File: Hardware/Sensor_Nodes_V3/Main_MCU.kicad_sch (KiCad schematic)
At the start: 21 parts, among them J2 Conn_01x27_Socket, J3 Conn_01x27_Socket, U2 STM32G474RBTx, U3 MCP2542FDxMF, U4 MCP2542FDxMF

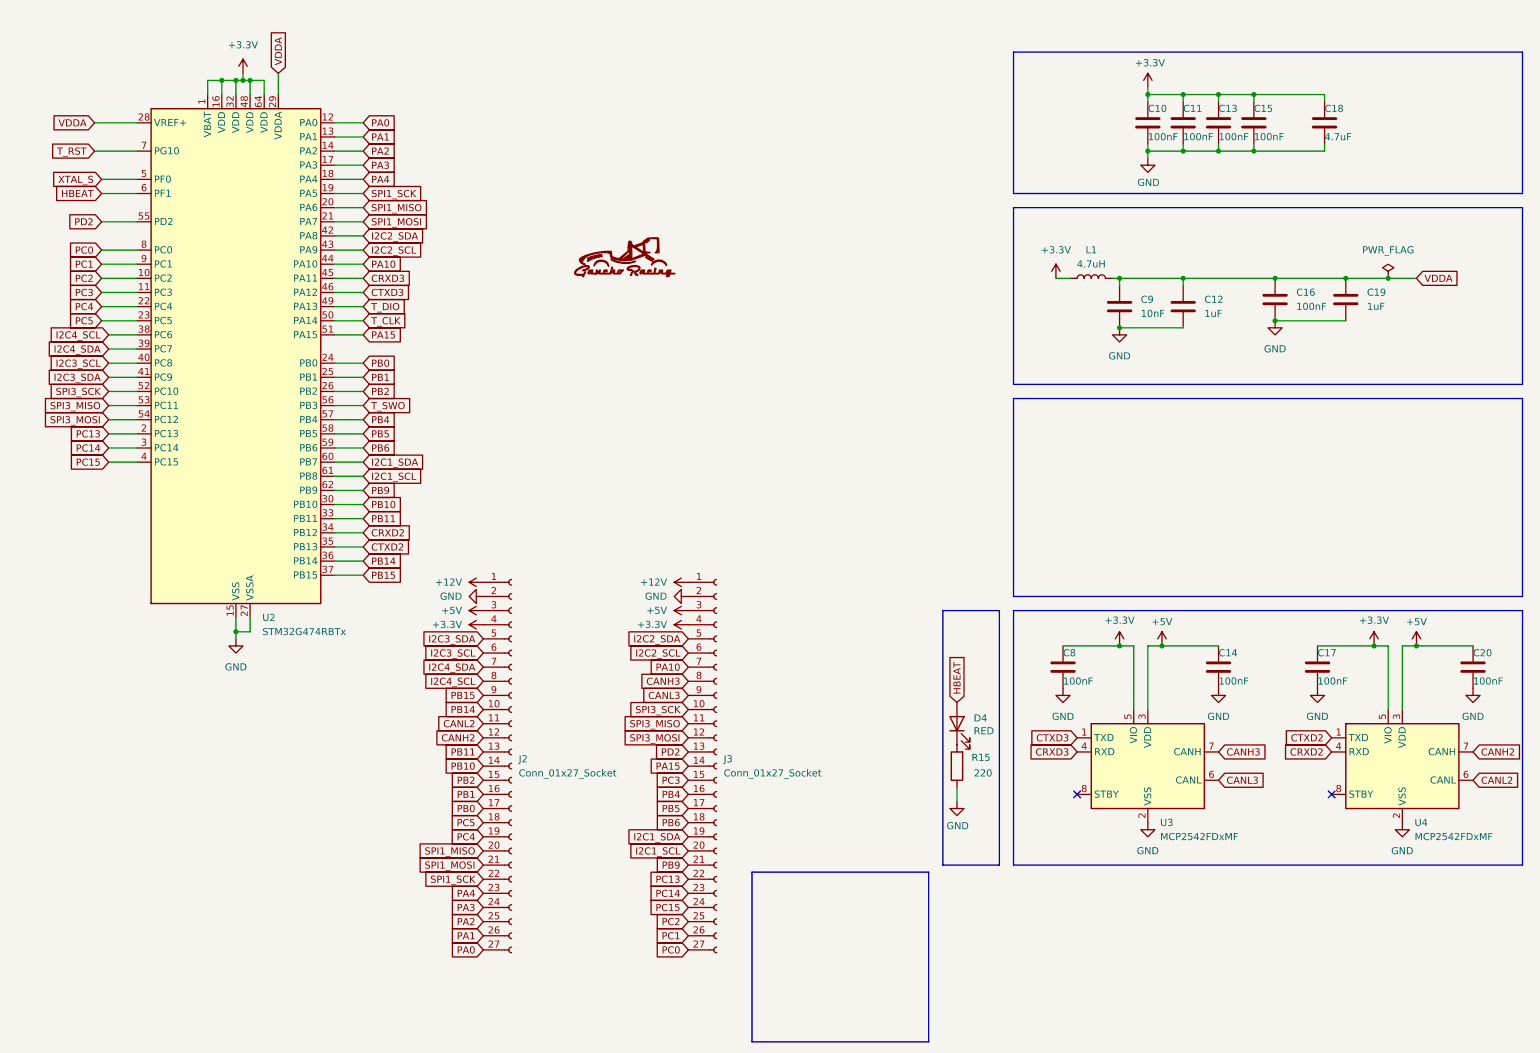
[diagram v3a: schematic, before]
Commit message: fixed placement, added some decals, now using clock from stlink
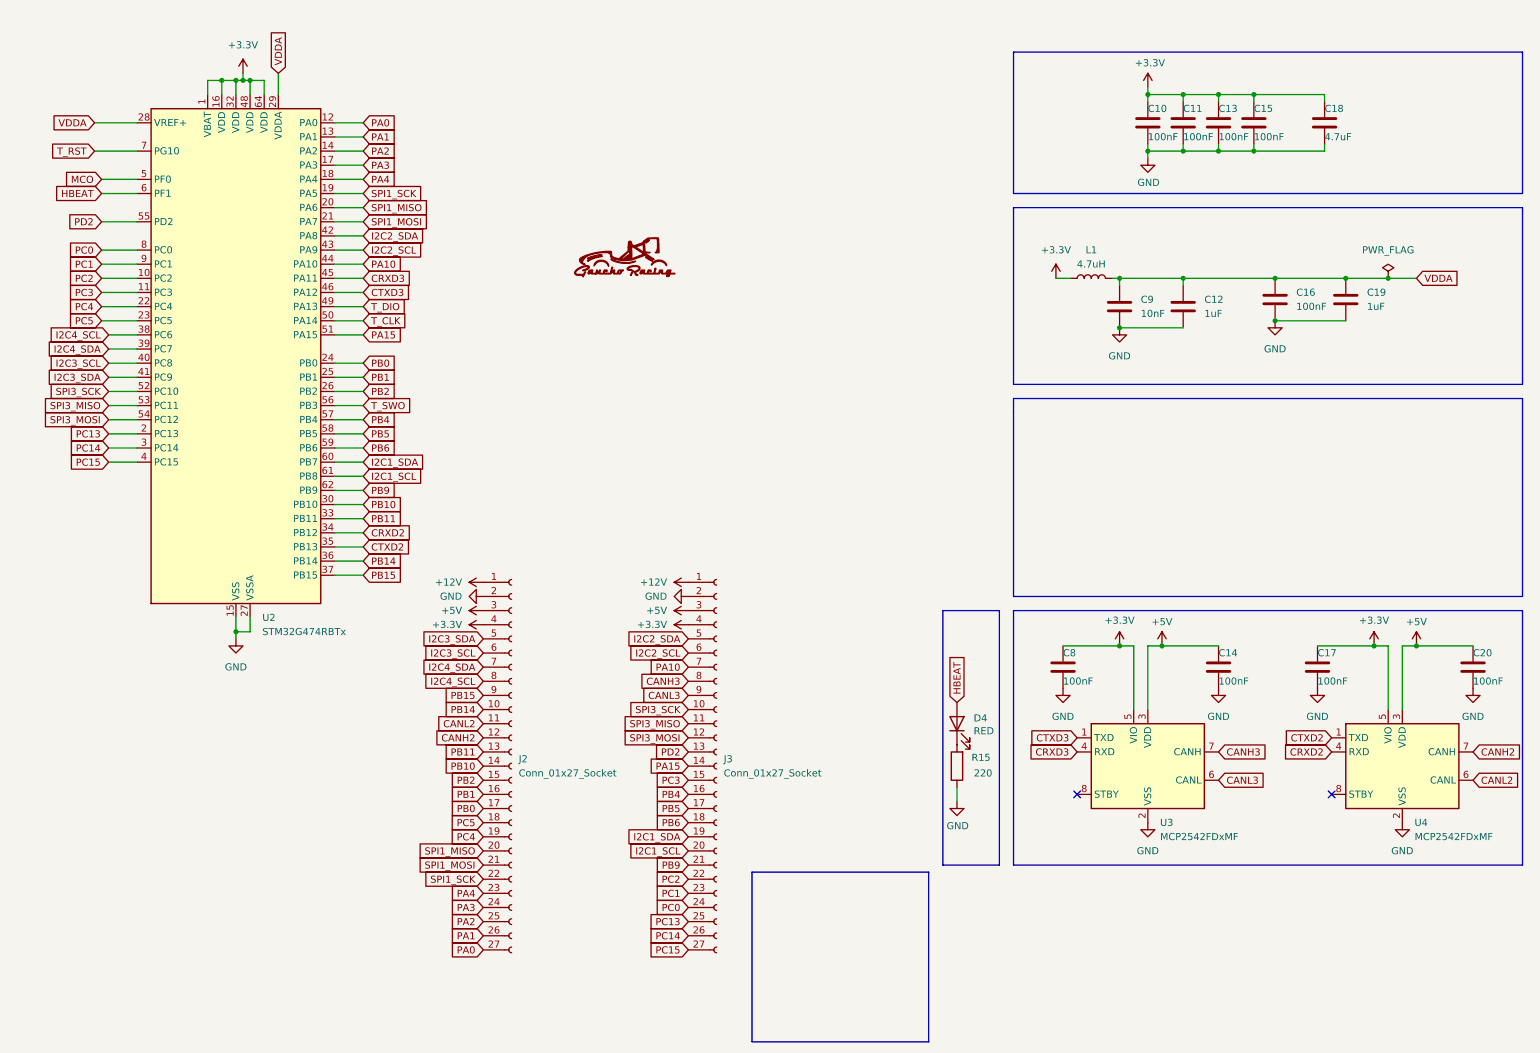
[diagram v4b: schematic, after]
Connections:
- net PC0: now also J3.24 (Pin_24); no longer J3.27 (Pin_27)
- net PC1: now also J3.23 (Pin_23); no longer J3.26 (Pin_26)
- net PC13: now also J3.25 (Pin_25); no longer J3.22 (Pin_22)
- net PC14: now also J3.26 (Pin_26); no longer J3.23 (Pin_23)
- net PC15: now also J3.27 (Pin_27); no longer J3.24 (Pin_24)
- net PC2: now also J3.22 (Pin_22); no longer J3.25 (Pin_25)
- net XTAL_S renamed MCO

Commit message: fixed the CAN issue and rerouted some things. Added a solder bridge for Vref so that there is a choice of using it or not.
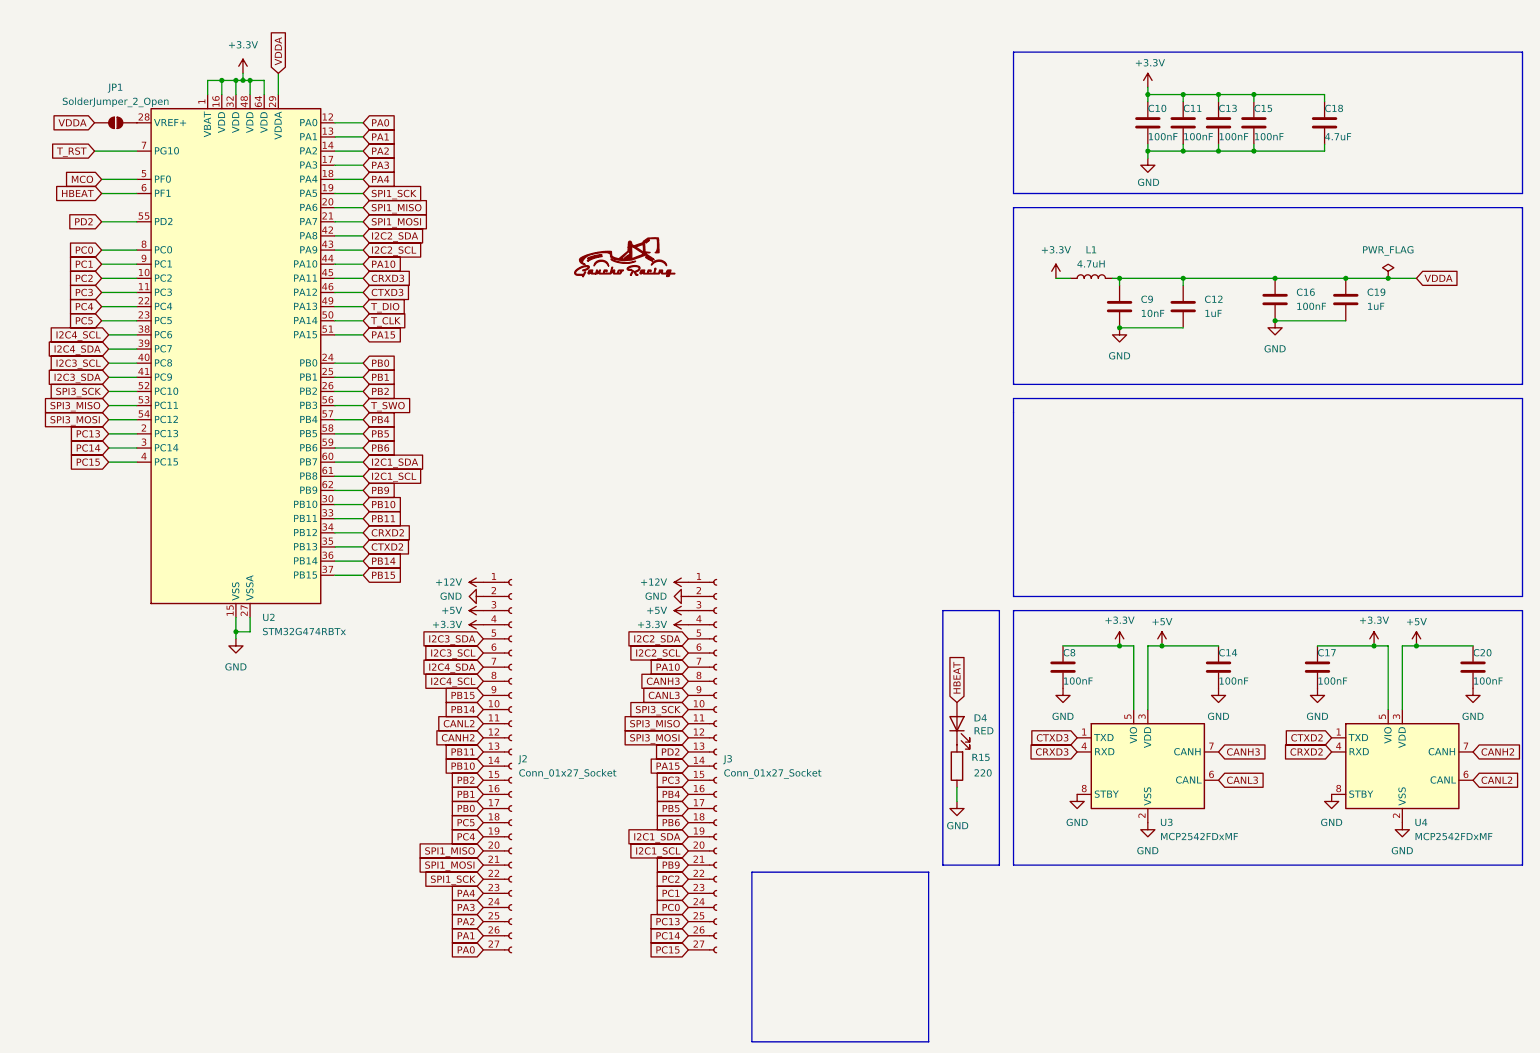
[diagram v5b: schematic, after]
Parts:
- added JP1: SolderJumper_2_Open, Jumper:SolderJumper-2_P1.3mm_Open_TrianglePad1.0x1.5mm, symbol Jumper:SolderJumper_2_Open
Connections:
- net GND: now also U3.8 (STBY), U4.8 (STBY)
- net VDDA: now also JP1.1 (A); no longer U2.28 (VREF+)
- new net: JP1.2 (B), U2.28 (VREF+)
- no-connect marks 2 -> 0
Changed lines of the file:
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@@
 		(color 0 0 0 0)
 	)
-	(no_connect
-		(at 247.65 152.4)
-	)
-	(no_connect
-		(at 201.93 152.4)
-	)
 	(wire
 		(pts
@@
 		)
 	)
-	(wire
-		(pts
-			(xy 25.4 31.75) (xy 33.02 31.75)
-		)
-		(stroke
-			(width 0)
-			(type default)
-		)
-	)
 	(polyline
 		(pts
@@
 	)
 	(symbol
+		(lib_id "Jumper:SolderJumper_2_Open")
+		(at 29.21 31.75 0)
+		(unit 1)
+		(exclude_from_sim yes)
+		(in_bom no)
+		(on_board yes)
+		(dnp no)
+		(fields_autoplaced yes)
+		(property "Reference" "JP1"
+			(at 29.21 25.4 0)
+			(effects
+				(font
+					(size 1.27 1.27)
+				)
+			)
+		)
+		(property "Value" "SolderJumper_2_Open"
+			(at 29.21 27.94 0)
+			(effects
+				(font
+					(size 1.27 1.27)
+				)
+			)
+		)
+		(property "Footprint" "Jumper:SolderJumper-2_P1.3mm_Open_TrianglePad1.0x1.5mm"
+			(at 29.21 31.75 0)
+			(effects
+				(font
+					(size 1.27 1.27)
+				)
+				(hide yes)
+			)
+		)
+		(property "Datasheet" "~"
+			(at 29.21 31.75 0)
+			(effects
+				(font
+					(size 1.27 1.27)
+				)
+				(hide yes)
+			)
+		)
+		(property "Description" "Solder Jumper, 2-pole, open"
+			(at 29.21 31.75 0)
+			(effects
+				(font
+					(size 1.27 1.27)
+				)
+				(hide yes)
+			)
+		)
+		(pin "2"
+		)
+		(pin "1"
+		)
+		(instances
+			(project ""
+				(path "/7b4e8e38-4440-451f-8c12-a5c49d6e3525/466e2466-e768-4b2c-901e-6531e50d4122"
+					(reference "JP1")
+					(unit 1)
+				)
+			)
+		)
+	)
+	(symbol
 		(lib_id "Device:C")
 		(at 214.63 31.75 0)
@@
 	)
 	(symbol
+		(lib_id "power:GND")
+		(at 201.93 152.4 0)
+		(unit 1)
+		(exclude_from_sim no)
+		(in_bom yes)
+		(on_board yes)
+		(dnp no)
+		(fields_autoplaced yes)
+		(property "Reference" "#PWR056"
+			(at 201.93 158.75 0)
+			(effects
+				(font
+					(size 1.27 1.27)
+				)
+				(hide yes)
+			)
+		)
+		(property "Value" "GND"
+			(at 201.93 157.48 0)
+			(effects
+				(font
+					(size 1.27 1.27)
+				)
+			)
+		)
+		(property "Footprint" ""
+			(at 201.93 152.4 0)
+			(effects
+				(font
+					(size 1.27 1.27)
+				)
+				(hide yes)
+			)
+		)
+		(property "Datasheet" ""
+			(at 201.93 152.4 0)
+			(effects
+				(font
+					(size 1.27 1.27)
+				)
+				(hide yes)
+			)
+		)
+		(property "Description" "Power symbol creates a global label with name \"GND\" , ground"
+			(at 201.93 152.4 0)
+			(effects
+				(font
+					(size 1.27 1.27)
+				)
+				(hide yes)
+			)
+		)
+		(pin "1"
+		)
+		(instances
+			(project ""
+				(path "/7b4e8e38-4440-451f-8c12-a5c49d6e3525/466e2466-e768-4b2c-901e-6531e50d4122"
+					(reference "#PWR056")
+					(unit 1)
+				)
+			)
+		)
+	)
+	(symbol
 		(lib_id "Device:C")
 		(at 227.33 31.75 0)
@@
 					(unit 1)
 				)
+			)
+		)
+	)
+	(symbol
+		(lib_id "power:GND")
+		(at 247.65 152.4 0)
+		(unit 1)
+		(exclude_from_sim no)
+		(in_bom yes)
+		(on_board yes)
+		(dnp no)
+		(fields_autoplaced yes)
+		(property "Reference" "#PWR057"
+			(at 247.65 158.75 0)
+			(effects
+				(font
+					(size 1.27 1.27)
+				)
+				(hide yes)
+			)
+		)
+		(property "Value" "GND"
+			(at 247.65 157.48 0)
+			(effects
+				(font
+					(size 1.27 1.27)
+				)
+			)
+		)
+		(property "Footprint" ""
+			(at 247.65 152.4 0)
+			(effects
+				(font
+					(size 1.27 1.27)
+				)
+				(hide yes)
+			)
+		)
+		(property "Datasheet" ""
+			(at 247.65 152.4 0)
+			(effects
+				(font
+					(size 1.27 1.27)
+				)
+				(hide yes)
+			)
+		)
+		(property "Description" "Power symbol creates a global label with name \"GND\" , ground"
+			(at 247.65 152.4 0)
+			(effects
+				(font
+					(size 1.27 1.27)
+				)
+				(hide yes)
+			)
+		)
+		(pin "1"
+		)
+		(instances
+			(project ""
+				(path "/7b4e8e38-4440-451f-8c12-a5c49d6e3525/466e2466-e768-4b2c-901e-6531e50d4122"
+					(reference "#PWR057")
+					(unit 1)
+				)

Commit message: V3.2 SAM Board added, CHASSES TOF code added and some TCM-CAN stuff added
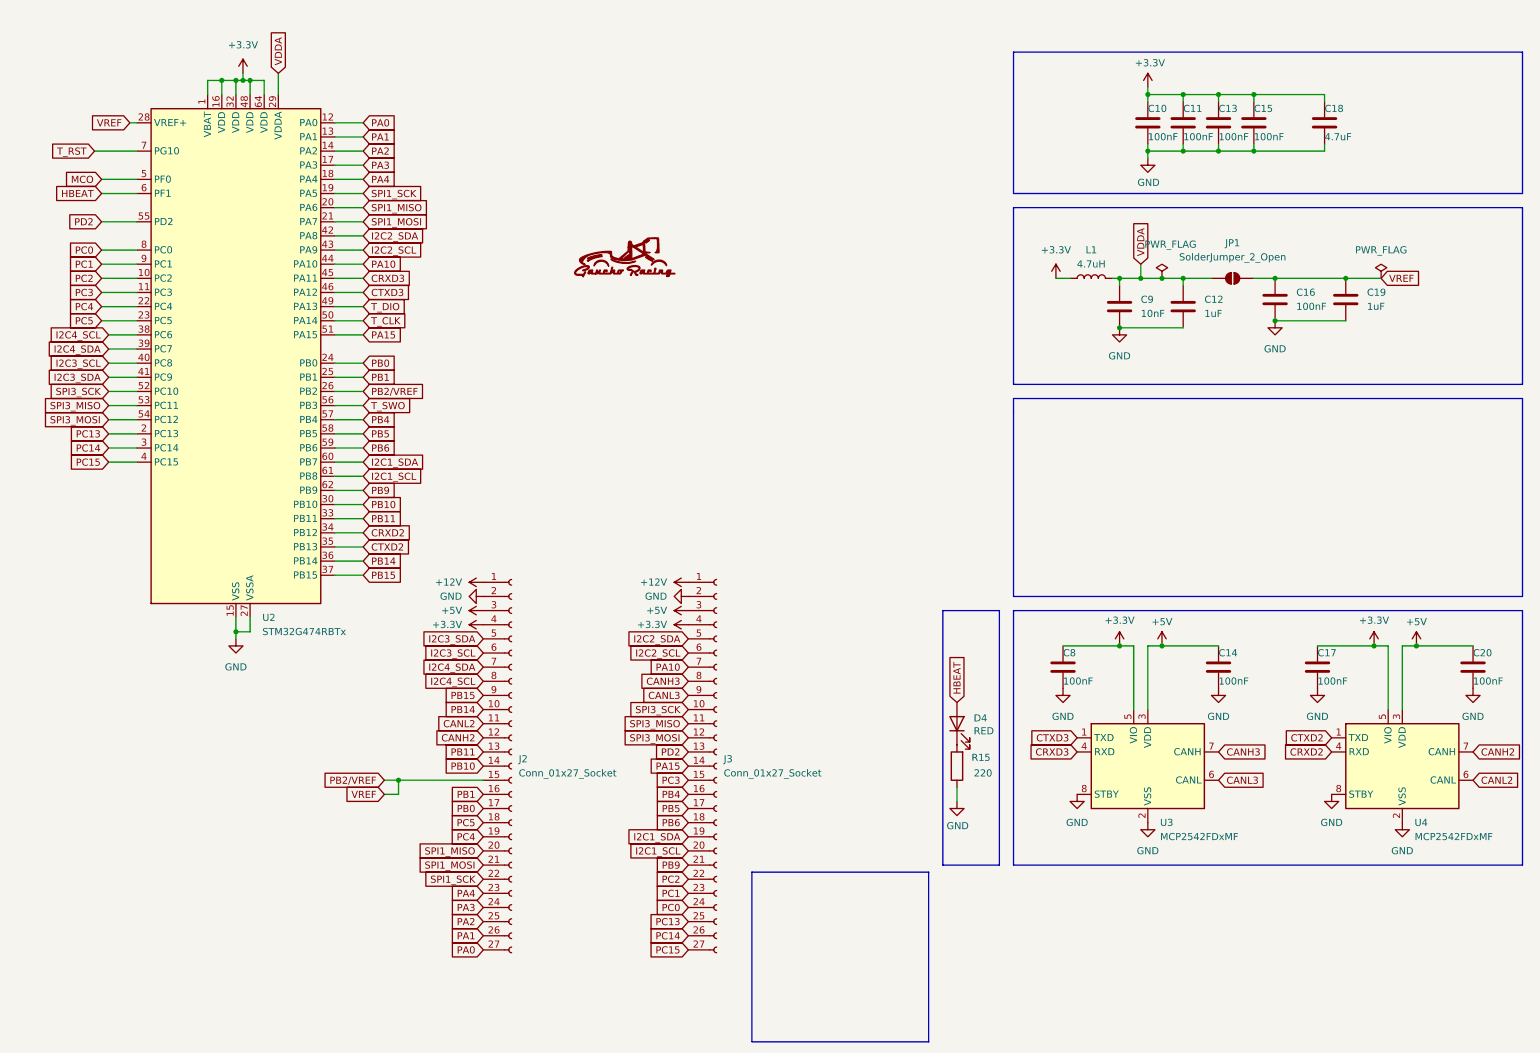
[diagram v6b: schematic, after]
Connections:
- net PB2 is gone; now on net PB2/VREF: J2.15 (Pin_15), U2.26 (PB2)
- net VDDA: no longer C16.1, C19.1
- net PB2/VREF: now reaches JP1.2 (B), U2.28 (VREF+)
- net PB2/VREF: now also C16.1, C19.1

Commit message: tcm can schematic done, only needs to be routed
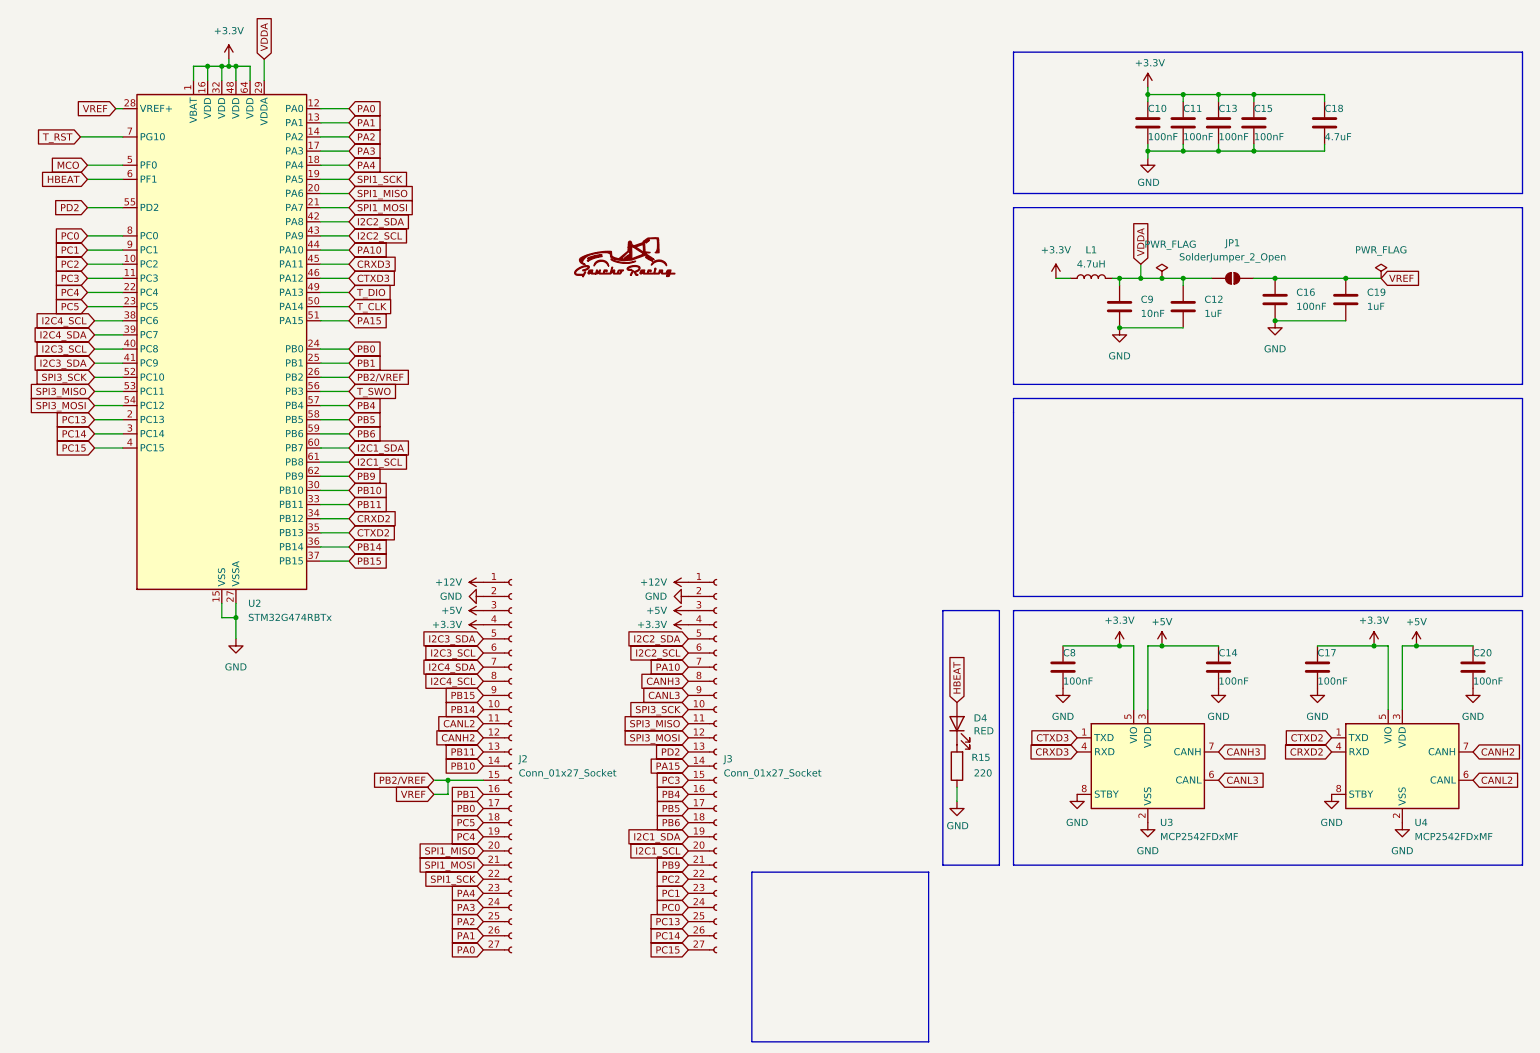
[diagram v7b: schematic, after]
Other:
- moved on the sheet: U2
